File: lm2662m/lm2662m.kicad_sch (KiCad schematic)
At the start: 0 parts

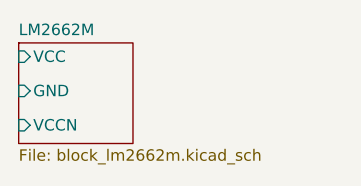
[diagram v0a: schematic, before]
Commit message: [Rushil] changed vccn to vee
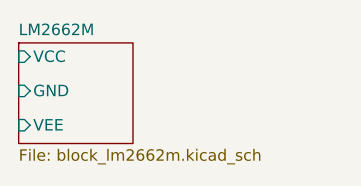
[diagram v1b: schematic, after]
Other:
- sheet LM2662M ports: added VEE; removed VCCN
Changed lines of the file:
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@@
 			)
 		)
-		(pin "VCCN" input
+		(pin "VEE" input
 			(at 115.062 90.17 180)
 			(effects
